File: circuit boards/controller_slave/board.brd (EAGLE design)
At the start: 85.1 x 67 mm, 60 parts, among them IC1 74HC595N, IC2 74HC595N, IC3 74HC595N, IC4 7805TV, Q1 14,7456, U1 ATTINY85-20P, X1 MKDSN1,5/2-5,08, X2 MKDSN1,5/2-5,08, X3 MKDSN1,5/2-5,08

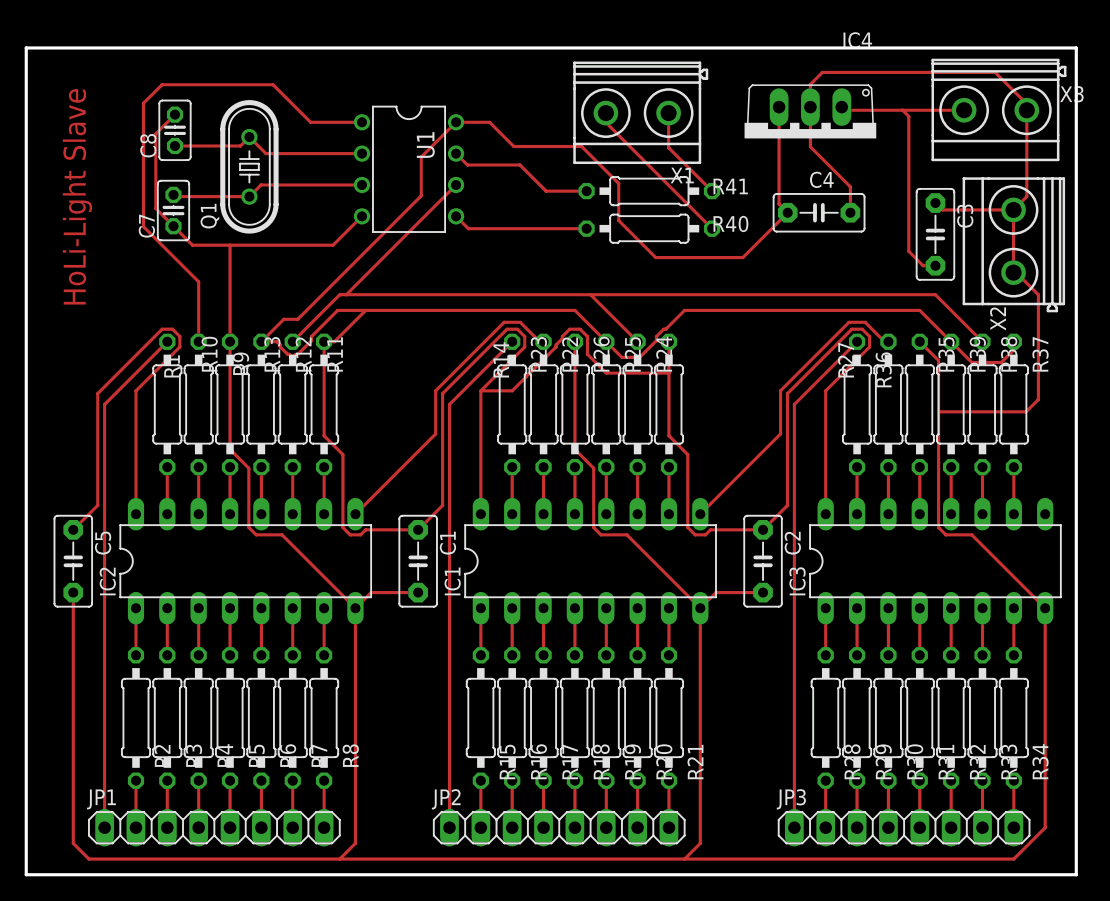
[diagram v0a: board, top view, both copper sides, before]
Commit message: changed PCB: mostly SMD parts
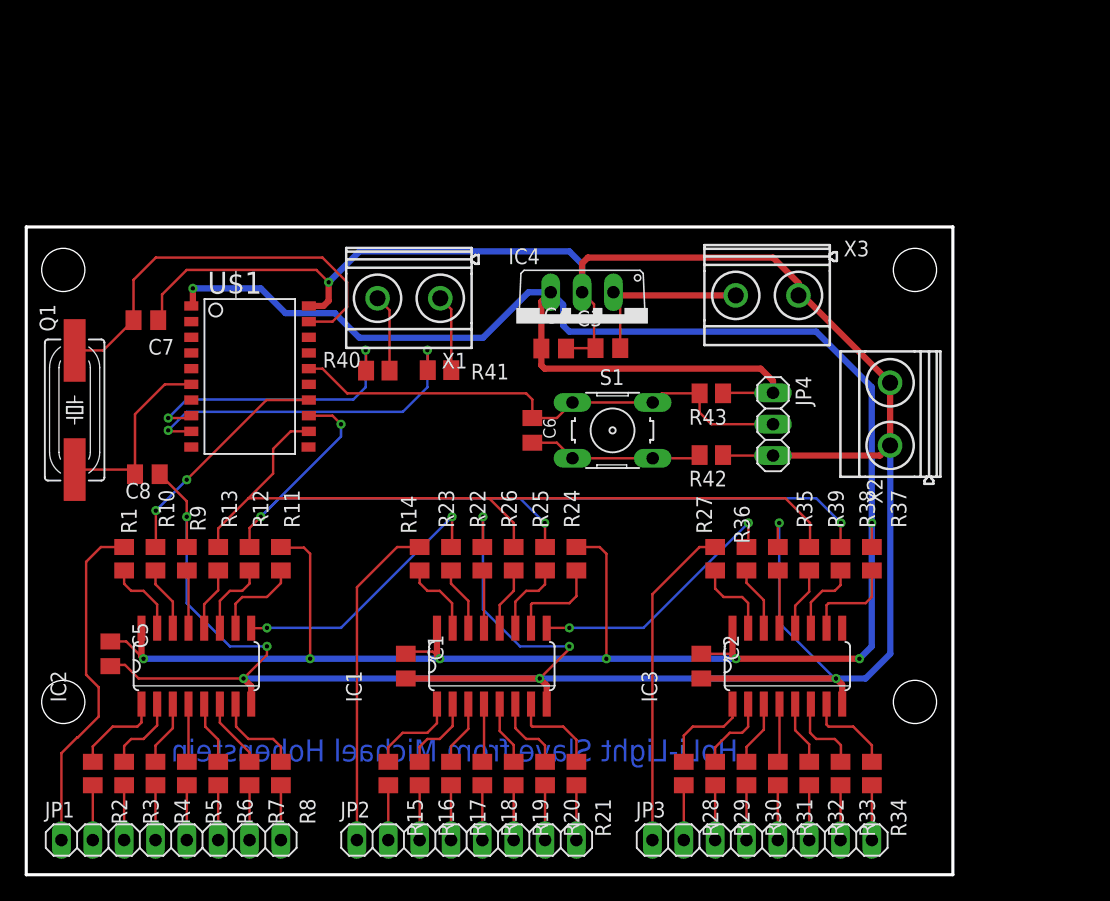
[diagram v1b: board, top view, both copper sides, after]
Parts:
- removed U1: ATTINY85-20P, attiny25_45_85:PDIP08_300MIL
- added C6: 100n, rcl:C0805K
- added JP4: (no value), pinhead:1X03
- added R42: 1K, resistor:M0805
- added R43: 10K, resistor:M0805
- added S1: (no value), switch-omron:B3F-10XX
- added U$1: ATTINY406, My_AVRs:SO20L
- C1, C2, C3, C4, C5: device capacitor-wima:C5B3 -> rcl:C0805K
- C7, C8: value 22pF -> 12pF; device resistor:C025-025X050 -> rcl:C0805K
- IC1, IC2, IC3: value 74HC595N -> 74HC595D; device 74xx-eu:DIL16 -> 74xx-eu:SO16
- Q1: device crystal:HC49/S -> crystal:SM49
- R1, R10, R11, R12, R13, R14, R15, R16, R17, R18, R19, R2, R20, R21, R22, R23, R24, R25, R26, R27, R28, R29, R3, R30, R31, R32, R33, R34, R35, R36, R37, R38, R39, R4, R5, R6, R7, R8, R9: device resistor:0207/10 -> resistor:M0805
- R40, R41: value 500 -> 100; device resistor:0207/10 -> resistor:M0805
- X1, X2, X3: value MKDSN1,5/2-5,08 -> (none)
- moved C3 28.1 mm to (47.1, 42.7), turned to 0 degrees
- moved C8 27.9 mm to (9.81, 32.5), turned to 0 degrees
- moved R40 24.8 mm to (28.5, 40.8)
- moved Q1 24.3 mm to (3.92, 37.6), turned to 270 degrees
- moved C4 24.2 mm to (42.7, 42.6)
- moved IC4 23.8 mm to (45.0, 44.6)
- moved X3 23.8 mm to (60.0, 47.0)
- moved X1 23.8 mm to (31.0, 46.7)
- moved R41 22.3 mm to (33.5, 40.9)
- moved X2 17.2 mm to (70.0, 37.3)
- moved R39 17.0 mm to (63.4, 25.6)
- moved R27 17.0 mm to (55.8, 25.6)
- moved R35 17.0 mm to (60.9, 25.6)
- moved R37 17.0 mm to (68.5, 25.6)
- moved R38 17.0 mm to (66.0, 25.6)
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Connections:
- new net N$68: R13.1, R26.1, R39.1, U$1.12
- new net N$75: C6.1, JP4.2, R43.2, S1.1, S1.2, U$1.16
- new net N$76: C6.2, R42.2, S1.3, S1.4
- net +5V: now also JP4.1, R43.1, U$1.1; no longer R13.1, R26.1, R39.1, U1.8
- net GND: now also JP4.3, R42.1, U$1.20; no longer U1.4
- net N$67: now also U$1.13; no longer U1.6
- net N$69: now also U$1.8; no longer U1.5
- net N$70: now also U$1.9; no longer U1.7
- net N$73: now also U$1.14; no longer U1.1
- net N$74: now also U$1.19; no longer U1.3
- net N$78: now also U$1.6; no longer U1.2
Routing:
- net +5V: track 318.3 -> 216.0 mm, vias 0 -> 8
- net GND: track 358.5 -> 276.6 mm, vias 0 -> 9
- net N$68: track 0.00 -> 66.4 mm
- net N$75: track 0.00 -> 42.9 mm
- net N$73: track 40.8 -> 19.1 mm, vias 0 -> 2
- net N$74: track 15.7 -> 33.5 mm
- net N$70: track 11.8 -> 29.0 mm, vias 0 -> 2
- net N$56: track 41.5 -> 26.6 mm
- net N$35: track 41.5 -> 26.9 mm
- net N$76: track 0.00 -> 14.2 mm
- net N$14: track 41.5 -> 27.8 mm
- net N$69: track 11.0 -> 23.7 mm, vias 0 -> 2
- net N$72: track 24.3 -> 14.8 mm
- net N$66: track 12.9 -> 6.27 mm
- net N$67: track 77.0 -> 71.1 mm, vias 0 -> 4
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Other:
- board size 85.1 x 67 mm -> 75.1 x 52.5 mm
- board text added: "GND"
- board text added: "HoLi-Light Slave from Michael Hohenstein"
- board text added: "Rx"
- board text added: "Tx"
- board text added: "VCC"
- board text removed: "HoLi-Light Slave"

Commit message: Controller Slave: Lastkapazität Quarz und UPDI Schnittstelle angepasst
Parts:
- C6: value 100n -> 4,7nF
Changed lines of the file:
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@@
 <drawing>
 <settings>
-<setting alwaysvectorfont="yes"/>
+<setting alwaysvectorfont="no"/>
 <setting verticaltext="up"/>
 </settings>
@@
 <attribute name="VALUE" x="57.325" y="40.31" size="1.27" layer="27" rot="R270"/>
 </element>
-<element name="C6" library="rcl" library_urn="urn:adsk.eagle:library:334" package="C0805K" package3d_urn="urn:adsk.eagle:package:23681/2" value="100n" x="41" y="36" smashed="yes" rot="R270">
+<element name="C6" library="rcl" library_urn="urn:adsk.eagle:library:334" package="C0805K" package3d_urn="urn:adsk.eagle:package:23681/2" value="4,7nF" x="41" y="36" smashed="yes" rot="R270">
 <attribute name="NAME" x="41.875" y="37" size="1.016" layer="25" rot="R270"/>
 <attribute name="POPULARITY" value="52" x="41" y="36" size="1.778" layer="27" rot="R270" display="off"/>
 <attribute name="SPICEPREFIX" value="C" x="41" y="36" size="1.778" layer="27" rot="R270" display="off"/>
-<attribute name="VALUE" x="39.1" y="37" size="1.016" layer="27" rot="R270"/>
+<attribute name="VALUE" x="38.6" y="37" size="1.016" layer="27" rot="R270"/>
 </element>
 <element name="R42" library="resistor" library_urn="urn:adsk.eagle:library:348" package="M0805" value="1K" x="55.5" y="34" smashed="yes" rot="R180">
